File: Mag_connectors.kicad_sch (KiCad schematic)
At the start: 0 parts

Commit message: eeprom fanned out
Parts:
- added JB1, JB2, JB3: 502352-0210, symbol 502352-0210:502352-0210
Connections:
- new net GND: JB1.MP1, JB1.MP2, JB2.MP1, JB2.MP2, JB3.MP1, JB3.MP2
- new net IN_1_N: JB1.2
- new net IN_1_P: JB1.1
- new net IN_2_N: JB2.2
- new net IN_2_P: JB2.1
- new net IN_3_N: JB3.2
- new net IN_3_P: JB3.1
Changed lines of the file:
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@@
 (kicad_sch (version 20211123) (generator eeschema)
   (paper "A4")
+  (junction (at 71.12 96.52) (diameter 0) (color 0 0 0 0)
+  )
+  (junction (at 60.96 52.07) (diameter 0) (color 0 0 0 0)
+  )
+  (junction (at 77.47 138.43) (diameter 0) (color 0 0 0 0)
+  )
+  (wire (pts (xy 77.47 138.43) (xy 82.55 138.43))
+    (stroke (width 0) (type default) (color 0 0 0 0))
+  )
+  (wire (pts (xy 60.96 49.53) (xy 60.96 52.07))
+    (stroke (width 0) (type default) (color 0 0 0 0))
+  )
+  (wire (pts (xy 77.47 138.43) (xy 77.47 139.7))
+    (stroke (width 0) (type default) (color 0 0 0 0))
+  )
+  (wire (pts (xy 71.12 96.52) (xy 71.12 99.06))
+    (stroke (width 0) (type default) (color 0 0 0 0))
+  )
+  (wire (pts (xy 71.12 96.52) (xy 76.2 96.52))
+    (stroke (width 0) (type default) (color 0 0 0 0))
+  )
+  (wire (pts (xy 60.96 52.07) (xy 64.77 52.07))
+    (stroke (width 0) (type default) (color 0 0 0 0))
+  )
+  (wire (pts (xy 60.96 52.07) (xy 60.96 53.34))
+    (stroke (width 0) (type default) (color 0 0 0 0))
+  )
+  (wire (pts (xy 71.12 93.98) (xy 71.12 96.52))
+    (stroke (width 0) (type default) (color 0 0 0 0))
+  )
+  (wire (pts (xy 76.2 93.98) (xy 71.12 93.98))
+    (stroke (width 0) (type default) (color 0 0 0 0))
+  )
+  (wire (pts (xy 82.55 135.89) (xy 77.47 135.89))
+    (stroke (width 0) (type default) (color 0 0 0 0))
+  )
+  (wire (pts (xy 77.47 135.89) (xy 77.47 138.43))
+    (stroke (width 0) (type default) (color 0 0 0 0))
+  )
+  (wire (pts (xy 64.77 49.53) (xy 60.96 49.53))
+    (stroke (width 0) (type default) (color 0 0 0 0))
+  )
+  (hierarchical_label "IN_3_P" (shape output) (at 105.41 135.89 0)
+    (effects (font (size 1.27 1.27)) (justify left))
+  )
+  (hierarchical_label "IN_1_N" (shape output) (at 87.63 52.07 0)
+    (effects (font (size 1.27 1.27)) (justify left))
+  )
+  (hierarchical_label "IN_1_P" (shape output) (at 87.63 49.53 0)
+    (effects (font (size 1.27 1.27)) (justify left))
+  )
+  (hierarchical_label "IN_2_N" (shape output) (at 99.06 96.52 0)
+    (effects (font (size 1.27 1.27)) (justify left))
+  )
+  (hierarchical_label "IN_2_P" (shape output) (at 99.06 93.98 0)
+    (effects (font (size 1.27 1.27)) (justify left))
+  )
+  (hierarchical_label "IN_3_N" (shape output) (at 105.41 138.43 0)
+    (effects (font (size 1.27 1.27)) (justify left))
+  )
+  (symbol (lib_id "power:GND") (at 60.96 53.34 0) (unit 1)
+    (in_bom yes) (on_board yes) (fields_autoplaced)
+    (property "Reference" "#PWR?" (id 0) (at 60.96 59.69 0)
+      (effects (font (size 1.27 1.27)) hide)
+    )
+    (property "Value" "GND" (id 1) (at 60.96 58.42 0))
+    (property "Footprint" "" (id 2) (at 60.96 53.34 0)
+      (effects (font (size 1.27 1.27)) hide)
+    )
+    (property "Datasheet" "" (id 3) (at 60.96 53.34 0)
+      (effects (font (size 1.27 1.27)) hide)
+    )
+    (pin "1")
+  )
+  (symbol (lib_id "power:GND") (at 77.47 139.7 0) (unit 1)
+    (in_bom yes) (on_board yes) (fields_autoplaced)
+    (property "Reference" "#PWR?" (id 0) (at 77.47 146.05 0)
+      (effects (font (size 1.27 1.27)) hide)
+    )
+    (property "Value" "GND" (id 1) (at 77.47 144.78 0))
+    (property "Footprint" "" (id 2) (at 77.47 139.7 0)
+      (effects (font (size 1.27 1.27)) hide)
+    )
+    (property "Datasheet" "" (id 3) (at 77.47 139.7 0)
+      (effects (font (size 1.27 1.27)) hide)
+    )
+    (pin "1")
+  )
+  (symbol (lib_id "502352-0210:502352-0210") (at 64.77 49.53 0) (unit 1)
+    (in_bom yes) (on_board yes) (fields_autoplaced)
+    (property "Reference" "JB1" (id 0) (at 76.2 36.83 0))
+    (property "Value" "502352-0210" (id 1) (at 76.2 39.37 0))
+    (property "Footprint" "" (id 2) (at 64.77 49.53 0)
+      (effects (font (size 1.27 1.27)) hide)
+    )
+    (property "Datasheet" "" (id 3) (at 64.77 49.53 0)
+      (effects (font (size 1.27 1.27)) hide)
+    )
+    (property "Reference_1" "J" (id 4) (at 76.2 41.91 0))
+    (property "Value_1" "502352-0210" (id 5) (at 76.2 44.45 0))
+    (property "Footprint_1" "5023520210" (id 6) (at 83.82 144.45 0)
+      (effects (font (size 1.27 1.27)) (justify left top) hide)
+    )
+    (property "Datasheet_1" "https://componentsearchengine.com/Datasheets/1/502352-0210.pdf" (id 7) (at 83.82 244.45 0)
+      (effects (font (size 1.27 1.27)) (justify left top) hide)
+    )
+    (property "Height" "6.4" (id 8) (at 83.82 444.45 0)
+      (effects (font (size 1.27 1.27)) (justify left top) hide)
+    )
+    (property "Mouser Part Number" "538-502352-0210" (id 9) (at 83.82 544.45 0)
+      (effects (font (size 1.27 1.27)) (justify left top) hide)
+    )
+    (property "Mouser Price/Stock" "https://www.mouser.co.uk/ProductDetail/Molex/502352-0210?qs=yd8XiKYcH9lys38VlWdUCA%3D%3D" (id 10) (at 83.82 644.45 0)
+      (effects (font (size 1.27 1.27)) (justify left top) hide)
+    )
+    (property "Manufacturer_Name" "Molex" (id 11) (at 83.82 744.45 0)
+      (effects (font (size 1.27 1.27)) (justify left top) hide)
+    )
+    (property "Manufacturer_Part_Number" "502352-0210" (id 12) (at 83.82 844.45 0)
+      (effects (font (size 1.27 1.27)) (justify left top) hide)
+    )
+    (pin "1")
+    (pin "2")
+    (pin "MP1")
+    (pin "MP2")
+  )
+  (symbol (lib_id "502352-0210:502352-0210") (at 82.55 135.89 0) (unit 1)
+    (in_bom yes) (on_board yes) (fields_autoplaced)
+    (property "Reference" "JB3" (id 0) (at 93.98 123.19 0))
+    (property "Value" "502352-0210" (id 1) (at 93.98 125.73 0))
+    (property "Footprint" "" (id 2) (at 82.55 135.89 0)
+      (effects (font (size 1.27 1.27)) hide)
+    )
+    (property "Datasheet" "" (id 3) (at 82.55 135.89 0)
+      (effects (font (size 1.27 1.27)) hide)
+    )
+    (property "Reference_1" "J" (id 4) (at 93.98 128.27 0))
+    (property "Value_1" "502352-0210" (id 5) (at 93.98 130.81 0))
+    (property "Footprint_1" "5023520210" (id 6) (at 101.6 230.81 0)
+      (effects (font (size 1.27 1.27)) (justify left top) hide)
+    )
+    (property "Datasheet_1" "https://componentsearchengine.com/Datasheets/1/502352-0210.pdf" (id 7) (at 101.6 330.81 0)
+      (effects (font (size 1.27 1.27)) (justify left top) hide)
+    )
+    (property "Height" "6.4" (id 8) (at 101.6 530.81 0)
+      (effects (font (size 1.27 1.27)) (justify left top) hide)
+    )
+    (property "Mouser Part Number" "538-502352-0210" (id 9) (at 101.6 630.81 0)
+      (effects (font (size 1.27 1.27)) (justify left top) hide)
+    )
+    (property "Mouser Price/Stock" "https://www.mouser.co.uk/ProductDetail/Molex/502352-0210?qs=yd8XiKYcH9lys38VlWdUCA%3D%3D" (id 10) (at 101.6 730.81 0)
+      (effects (font (size 1.27 1.27)) (justify left top) hide)
+    )
+    (property "Manufacturer_Name" "Molex" (id 11) (at 101.6 830.81 0)
+      (effects (font (size 1.27 1.27)) (justify left top) hide)
+    )
+    (property "Manufacturer_Part_Number" "502352-0210" (id 12) (at 101.6 930.81 0)
+      (effects (font (size 1.27 1.27)) (justify left top) hide)
+    )
+    (pin "1")
+    (pin "2")
+    (pin "MP1")
+    (pin "MP2")
+  )
+  (symbol (lib_id "502352-0210:502352-0210") (at 76.2 93.98 0) (unit 1)
+    (in_bom yes) (on_board yes) (fields_autoplaced)
+    (property "Reference" "JB2" (id 0) (at 87.63 81.28 0))
+    (property "Value" "502352-0210" (id 1) (at 87.63 83.82 0))
+    (property "Footprint" "" (id 2) (at 76.2 93.98 0)
+      (effects (font (size 1.27 1.27)) hide)
+    )
+    (property "Datasheet" "" (id 3) (at 76.2 93.98 0)
+      (effects (font (size 1.27 1.27)) hide)
+    )
+    (property "Reference_1" "J" (id 4) (at 87.63 86.36 0))
+    (property "Value_1" "502352-0210" (id 5) (at 87.63 88.9 0))
+    (property "Footprint_1" "5023520210" (id 6) (at 95.25 188.9 0)
+      (effects (font (size 1.27 1.27)) (justify left top) hide)
+    )
+    (property "Datasheet_1" "https://componentsearchengine.com/Datasheets/1/502352-0210.pdf" (id 7) (at 95.25 288.9 0)
+      (effects (font (size 1.27 1.27)) (justify left top) hide)
+    )
+    (property "Height" "6.4" (id 8) (at 95.25 488.9 0)
+      (effects (font (size 1.27 1.27)) (justify left top) hide)
+    )
+    (property "Mouser Part Number" "538-502352-0210" (id 9) (at 95.25 588.9 0)
+      (effects (font (size 1.27 1.27)) (justify left top) hide)
+    )
+    (property "Mouser Price/Stock" "https://www.mouser.co.uk/ProductDetail/Molex/502352-0210?qs=yd8XiKYcH9lys38VlWdUCA%3D%3D" (id 10) (at 95.25 688.9 0)
+      (effects (font (size 1.27 1.27)) (justify left top) hide)
+    )
+    (property "Manufacturer_Name" "Molex" (id 11) (at 95.25 788.9 0)
+      (effects (font (size 1.27 1.27)) (justify left top) hide)
+    )
+    (property "Manufacturer_Part_Number" "502352-0210" (id 12) (at 95.25 888.9 0)
+      (effects (font (size 1.27 1.27)) (justify left top) hide)
+    )
+    (pin "1")
+    (pin "2")
+    (pin "MP1")
+    (pin "MP2")
+  )
+  (symbol (lib_id "power:GND") (at 71.12 99.06 0) (unit 1)
+    (in_bom yes) (on_board yes) (fields_autoplaced)
+    (property "Reference" "#PWR?" (id 0) (at 71.12 105.41 0)
+      (effects (font (size 1.27 1.27)) hide)
+    )
+    (property "Value" "GND" (id 1) (at 71.12 104.14 0))
+    (property "Footprint" "" (id 2) (at 71.12 99.06 0)
+      (effects (font (size 1.27 1.27)) hide)
+    )
+    (property "Datasheet" "" (id 3) (at 71.12 99.06 0)
+      (effects (font (size 1.27 1.27)) hide)
+    )
+    (pin "1")
+  )
 )

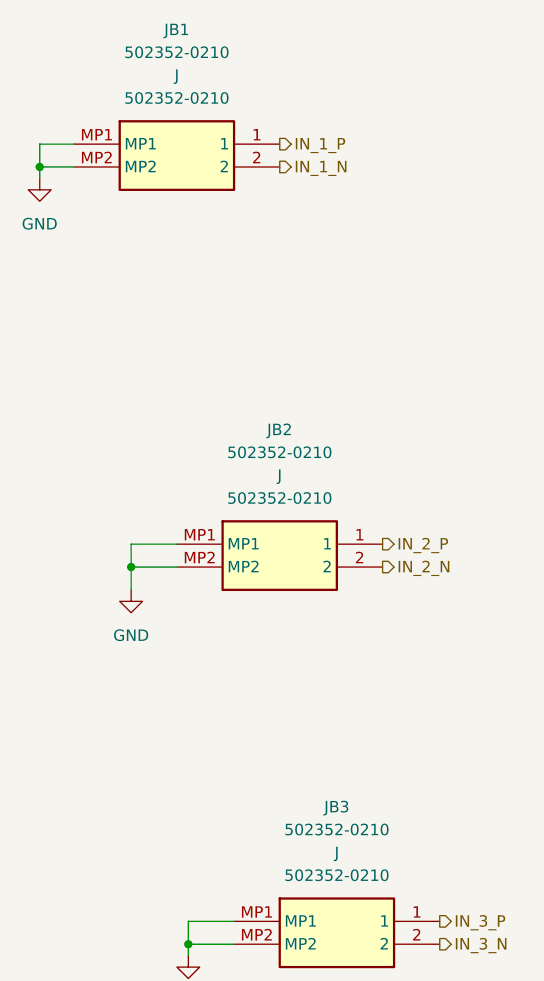
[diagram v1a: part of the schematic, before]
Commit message: all sheet designators added
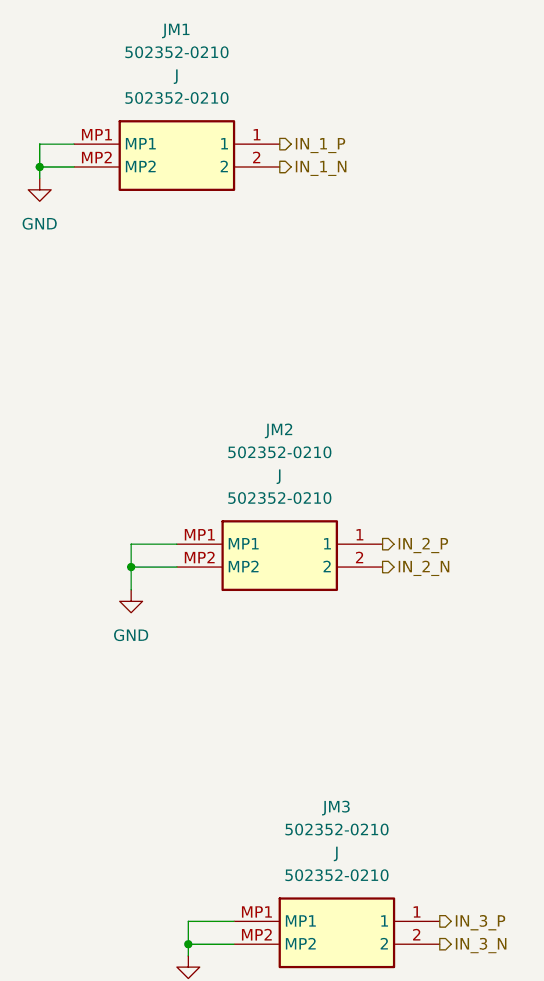
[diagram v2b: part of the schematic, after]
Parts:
- renumbered JB1 to JM1, JB2 to JM2, JB3 to JM3
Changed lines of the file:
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@@
   (symbol (lib_id "502352-0210:502352-0210") (at 64.77 49.53 0) (unit 1)
     (in_bom yes) (on_board yes) (fields_autoplaced)
-    (property "Reference" "JB1" (id 0) (at 76.2 36.83 0))
+    (property "Reference" "JM1" (id 0) (at 76.2 36.83 0))
     (property "Value" "502352-0210" (id 1) (at 76.2 39.37 0))
     (property "Footprint" "" (id 2) (at 64.77 49.53 0)
@@
   (symbol (lib_id "502352-0210:502352-0210") (at 82.55 135.89 0) (unit 1)
     (in_bom yes) (on_board yes) (fields_autoplaced)
-    (property "Reference" "JB3" (id 0) (at 93.98 123.19 0))
+    (property "Reference" "JM3" (id 0) (at 93.98 123.19 0))
     (property "Value" "502352-0210" (id 1) (at 93.98 125.73 0))
     (property "Footprint" "" (id 2) (at 82.55 135.89 0)
@@
   (symbol (lib_id "502352-0210:502352-0210") (at 76.2 93.98 0) (unit 1)
     (in_bom yes) (on_board yes) (fields_autoplaced)
-    (property "Reference" "JB2" (id 0) (at 87.63 81.28 0))
+    (property "Reference" "JM2" (id 0) (at 87.63 81.28 0))
     (property "Value" "502352-0210" (id 1) (at 87.63 83.82 0))
     (property "Footprint" "" (id 2) (at 76.2 93.98 0)

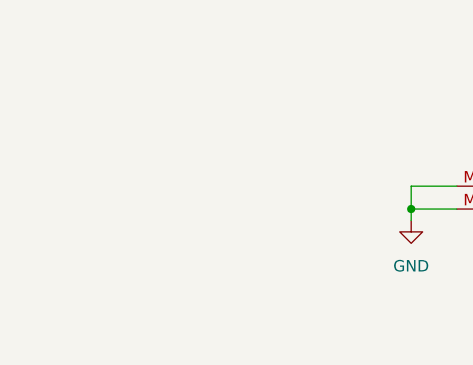
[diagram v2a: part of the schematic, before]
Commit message: MCU interfaces are done! Check the Changes and Complete ERC modifications
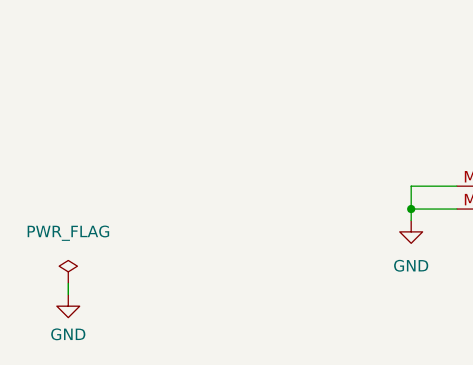
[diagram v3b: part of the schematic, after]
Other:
- company: (none) -> Parikshit Student Satellite Team
- title: (none) -> AOCS BOARD
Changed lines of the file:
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@@
 (kicad_sch (version 20211123) (generator eeschema)
   (paper "A4")
+  (title_block
+    (title "AOCS BOARD")
+    (company "Parikshit Student Satellite Team")
+  )
   (junction (at 71.12 96.52) (diameter 0) (color 0 0 0 0)
   )
@@
     (stroke (width 0) (type default) (color 0 0 0 0))
   )
+  (wire (pts (xy 39.37 147.955) (xy 39.37 146.685))
+    (stroke (width 0) (type default) (color 0 0 0 0))
+  )
   (wire (pts (xy 71.12 93.98) (xy 71.12 96.52))
     (stroke (width 0) (type default) (color 0 0 0 0))
@@
   (symbol (lib_id "power:GND") (at 60.96 53.34 0) (unit 1)
     (in_bom yes) (on_board yes) (fields_autoplaced)
-    (property "Reference" "#PWR?" (id 0) (at 60.96 59.69 0)
+    (property "Reference" "#PWR0250" (id 0) (at 60.96 59.69 0)
       (effects (font (size 1.27 1.27)) hide)
     )
@@
   (symbol (lib_id "power:GND") (at 77.47 139.7 0) (unit 1)
     (in_bom yes) (on_board yes) (fields_autoplaced)
-    (property "Reference" "#PWR?" (id 0) (at 77.47 146.05 0)
+    (property "Reference" "#PWR0252" (id 0) (at 77.47 146.05 0)
       (effects (font (size 1.27 1.27)) hide)
     )
@@
     (pin "MP2")
   )
+  (symbol (lib_id "power:GND") (at 39.37 147.955 0) (unit 1)
+    (in_bom yes) (on_board yes) (fields_autoplaced)
+    (property "Reference" "#PWR0279" (id 0) (at 39.37 154.305 0)
+      (effects (font (size 1.27 1.27)) hide)
+    )
+    (property "Value" "GND" (id 1) (at 39.37 152.4 0))
+    (property "Footprint" "" (id 2) (at 39.37 147.955 0)
+      (effects (font (size 1.27 1.27)) hide)
+    )
+    (property "Datasheet" "" (id 3) (at 39.37 147.955 0)
+      (effects (font (size 1.27 1.27)) hide)
+    )
+    (pin "1")
+  )
   (symbol (lib_id "502352-0210:502352-0210") (at 82.55 135.89 0) (unit 1)
     (in_bom yes) (on_board yes) (fields_autoplaced)
@@
   (symbol (lib_id "power:GND") (at 71.12 99.06 0) (unit 1)
     (in_bom yes) (on_board yes) (fields_autoplaced)
-    (property "Reference" "#PWR?" (id 0) (at 71.12 105.41 0)
+    (property "Reference" "#PWR0251" (id 0) (at 71.12 105.41 0)
       (effects (font (size 1.27 1.27)) hide)
     )
@@
       (effects (font (size 1.27 1.27)) hide)
     )
+    (pin "1")
+  )
+  (symbol (lib_id "power:PWR_FLAG") (at 39.37 146.685 0) (unit 1)
+    (in_bom yes) (on_board yes) (fields_autoplaced)
+    (property "Reference" "#FLG0115" (id 0) (at 39.37 144.78 0)
+      (effects (font (size 1.27 1.27)) hide)
+    )
+    (property "Value" "PWR_FLAG" (id 1) (at 39.37 140.97 0))
+    (property "Footprint" "" (id 2) (at 39.37 146.685 0)
+      (effects (font (size 1.27 1.27)) hide)
+    )
+    (property "Datasheet" "~" (id 3) (at 39.37 146.685 0)
+      (effects (font (size 1.27 1.27)) hide)
+    )

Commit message: added notes
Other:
- note added: "Check hmc 1051 pinout, lets keep two test points for the offset strap"
- note added: "We need 8 pin connector here"
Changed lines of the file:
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@@
     (stroke (width 0) (type default) (color 0 0 0 0))
+  )
+  (text "Check hmc 1051 \npinout, \nlets keep two test \npoints for the offset strap \n"
+    (at 154.94 76.2 0)
+    (effects (font (size 1.27 1.27)) (justify left bottom))
+  )
+  (text "We need 8 pin connector here \n" (at 154.94 67.31 0)
+    (effects (font (size 1.27 1.27)) (justify left bottom))
   )
   (hierarchical_label "IN_3_P" (shape output) (at 105.41 135.89 0)
